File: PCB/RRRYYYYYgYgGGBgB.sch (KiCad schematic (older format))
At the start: 46 parts, among them U1 74HC595, U2 74HC595

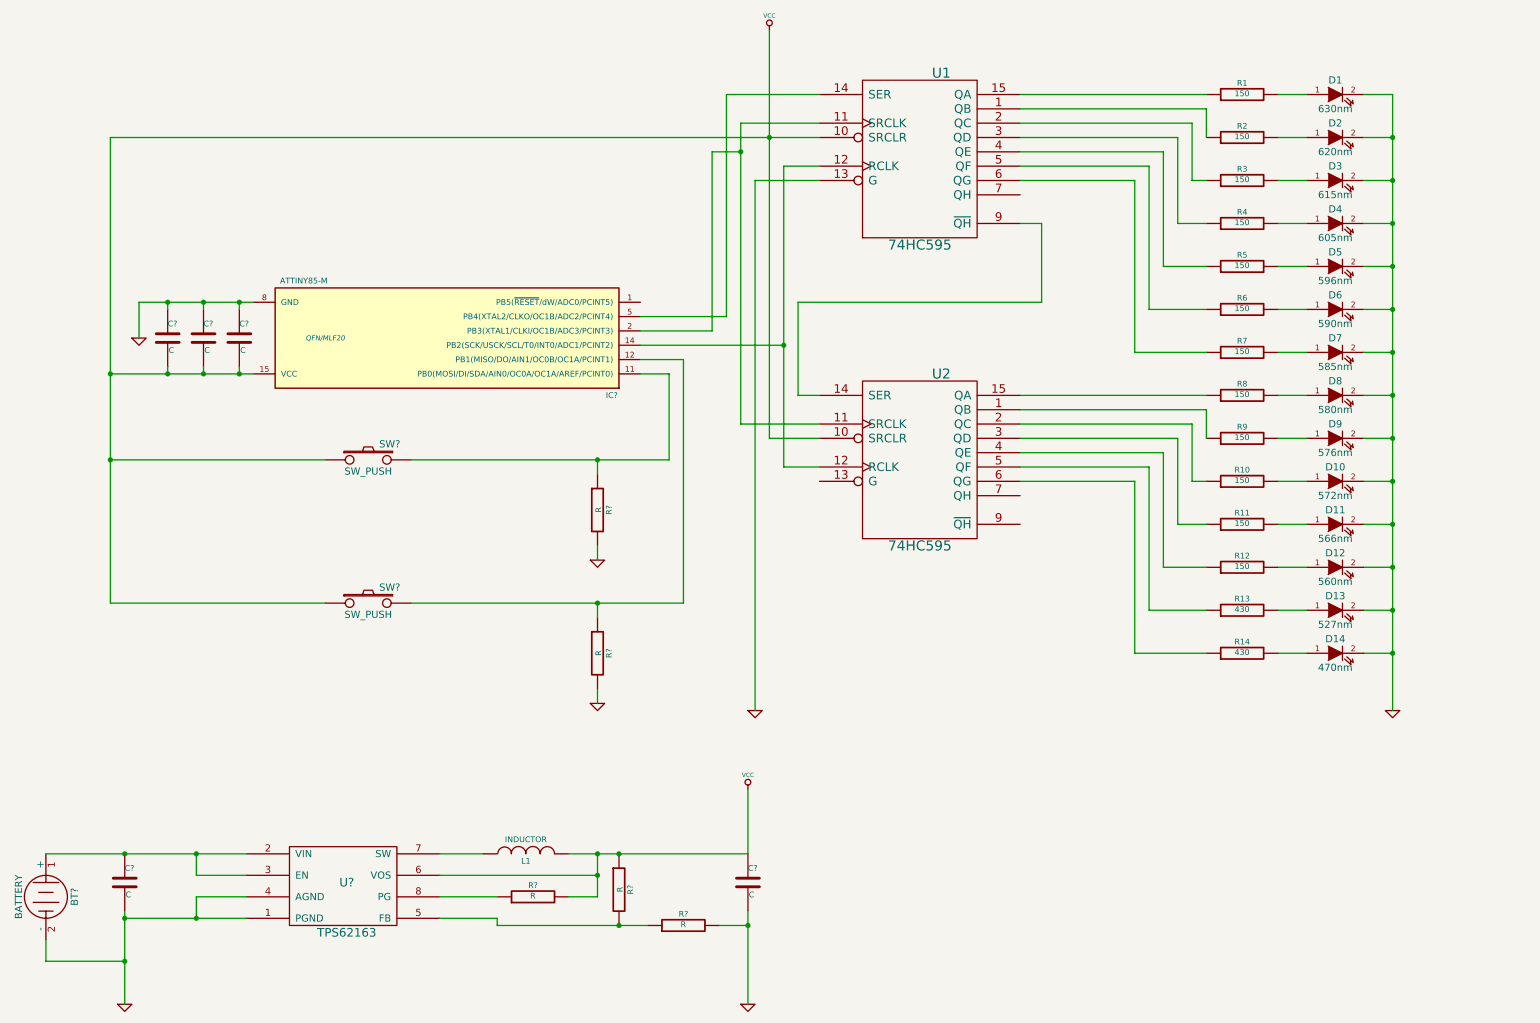
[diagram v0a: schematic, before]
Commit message: Changed from buck to boost converter for 3vdc power. Added values and designators for various components. Generated a netlist. More changes (likely) to come.
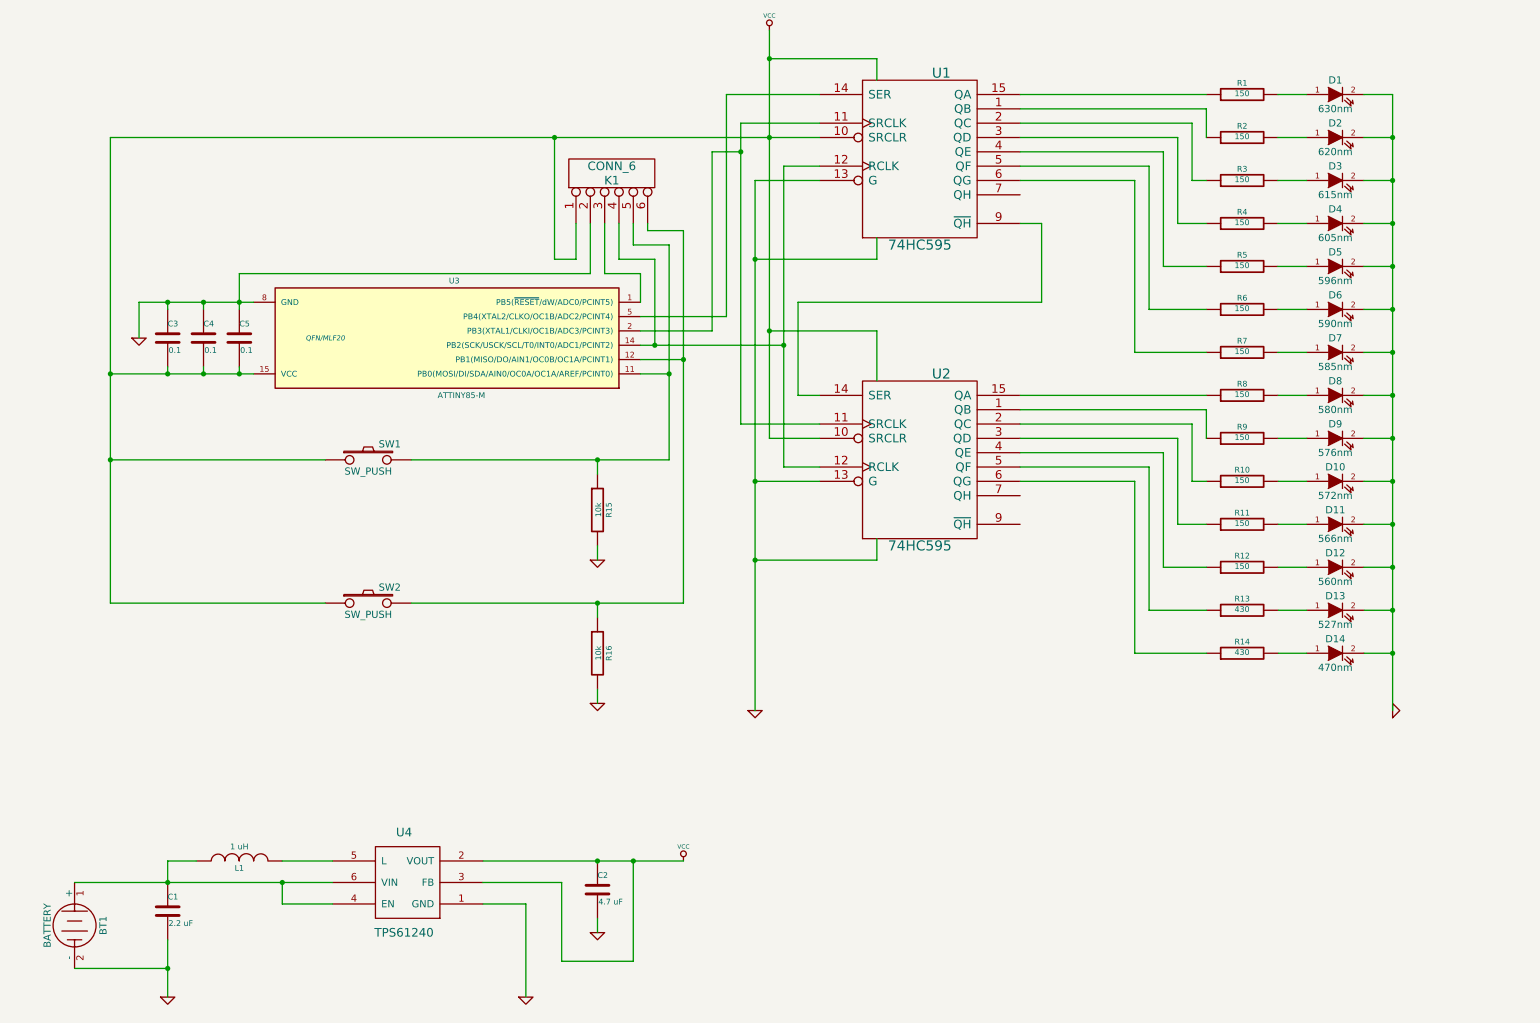
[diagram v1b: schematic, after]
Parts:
- removed BT?: BATTERY, ~, symbol BATTERY
- removed C? (x2): C, ~, symbol C
- removed R? (x3): R, ~, symbol R
- removed U?: TPS62163, symbol TPS62163
- added BT1: BATTERY, ~, symbol BATTERY
- added C1: 2.2 uF, ~, symbol C
- added C2: 4.7 uF, ~, symbol C
- added K1: CONN_6, symbol CONN_6
- added U4: TPS61240, symbol TPS61240
- C3, C4, C5: renamed from C?; value C -> 0.1
- L1: value INDUCTOR -> 1 uH
- R15, R16: renamed from R?; value R -> 10k
- gave numbers to parts that had none: 3
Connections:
- net GND: now also U2.13 (G), BT1.2 (-), C1.2, C2.2, K1.2, U4.1 (GND)
- net VCC: now also C2.1, K1.1, U4.2 (VOUT), U4.3 (FB); no longer L1.2
- net at U1.12 (RCLK), U2.12 (RCLK), U3.14 (PB2(SCK/USCK/SCL/T0/INT0/ADC1/PCINT2)): now also K1.4
- net at U3.1 (PB5(~RESET~/dW/ADC0/PCINT5)): now also K1.3
- net at R15.1, SW1.2, U3.11 (PB0(MOSI/DI/SDA/AIN0/OC0A/OC1A/AREF/PCINT0)): now also K1.5
- net at R16.1, SW2.2, U3.12 (PB1(MISO/DO/AIN1/OC0B/OC1A/PCINT1)): now also K1.6
- net at L1.1: now also BT1.1 (+), C1.1, U4.4 (EN), U4.6 (VIN)
- new net: L1.2, U4.5 (L)

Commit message: added pink and white LEDs. started pcb layout. LEDs arranged in an ~80 degree arc. schematic changed around a bit to make routing a tiny bit easier. note: schematic (specifically around shift registers and LEDs) is now quite difficult to read.
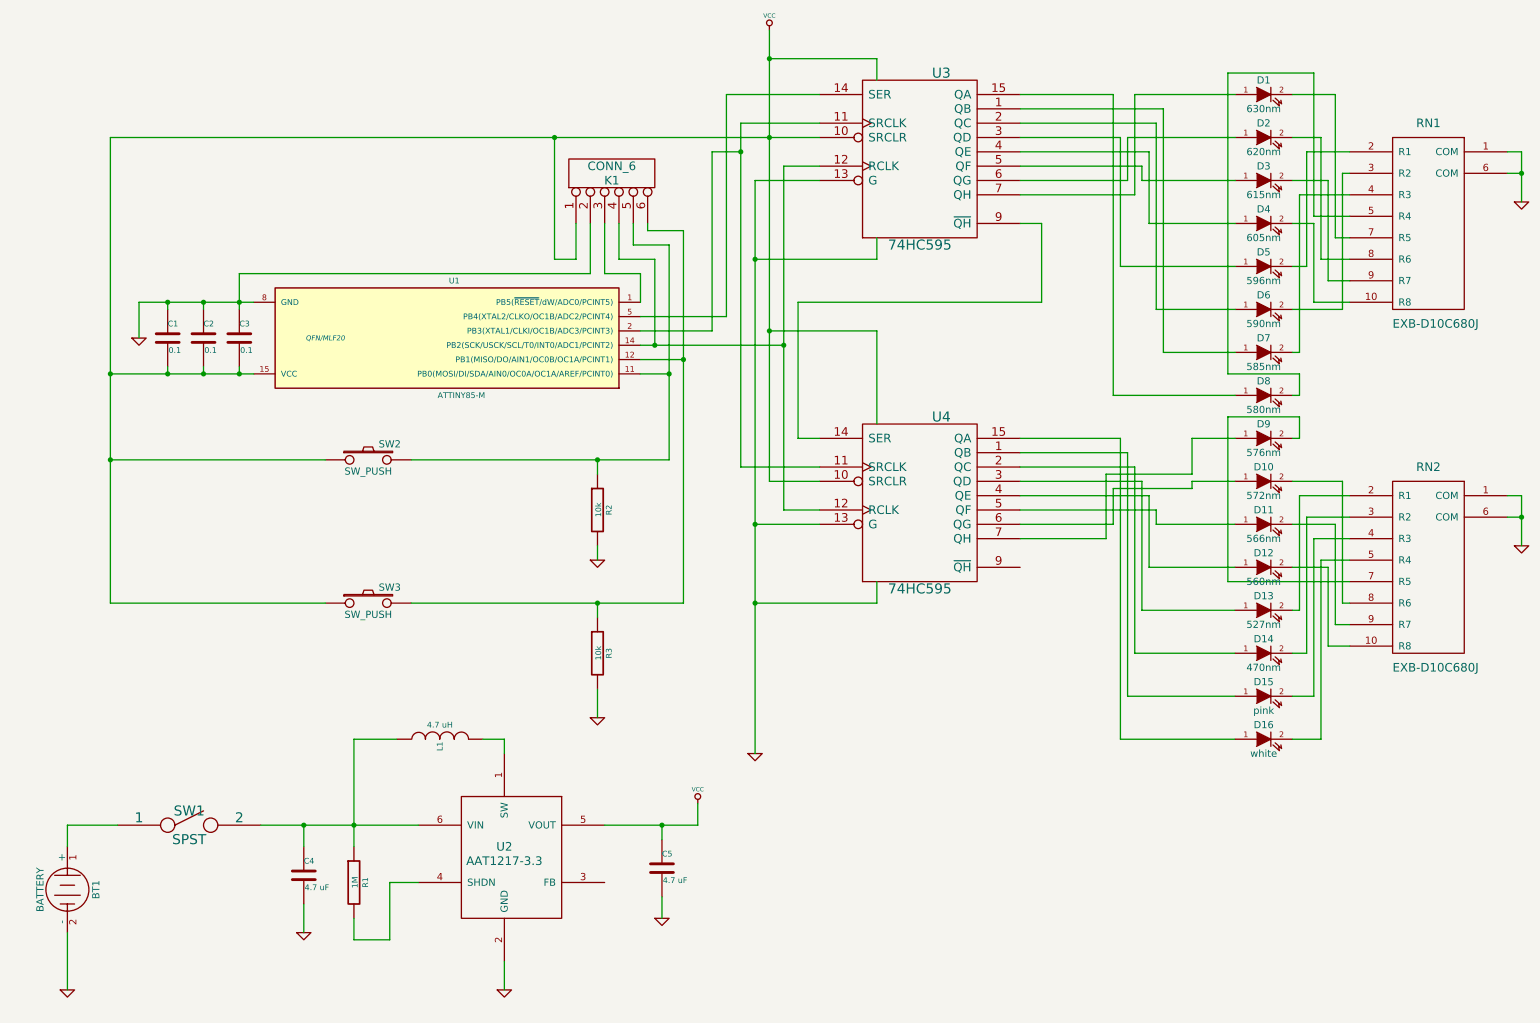
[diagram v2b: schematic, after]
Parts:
- removed C1: 2.2 uF, ~, symbol C
- removed C2: 4.7 uF, ~, symbol C
- removed R10, R11, R12, R2, R3, R4, R5, R6, R7, R8, R9: 150, ~, symbol R
- removed R13, R14: 430, ~, symbol R
- removed U4: TPS61240, symbol TPS61240
- added C4, C5: 4.7 uF, ~, symbol C
- added D15: pink, ~, symbol LED
- added D16: white, ~, symbol LED
- added RN1, RN2: EXB-D10C680J, symbol EXB-D10C680J
- added SW1: SPST, ~, symbol SPST
- added U2: AAT1217-3.3, symbol AAT1217-3.3
- L1: value 1 uH -> 4.7 uH
- R1: value 150 -> 1M
- renumbered C3 to C1, C4 to C2, C5 to C3, R15 to R2, R16 to R3, SW1 to SW2, SW2 to SW3, U3 to U1, U1 to U3, U2 to U4
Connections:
- net GND: now also C4.2, C5.2, RN1.1 (COM), RN1.6 (COM), RN2.1 (COM), RN2.6 (COM), U2.2 (GND); no longer D1.2 (K), D10.2 (K), D11.2 (K), D12.2 (K), D13.2 (K), D14.2 (K), D2.2 (K), D3.2 (K), D4.2 (K), D5.2 (K), D6.2 (K), D7.2 (K), D8.2 (K), D9.2 (K)
- net VCC: now also C5.1, U2.5 (VOUT)
- net at D7.1 (A): now also U3.1 (QB)
- net at D1.1 (A): now also U3.7 (QH); no longer R1.2
- net at D2.1 (A): now also U3.6 (QG)
- net at D3.1 (A): now also U3.5 (QF)
- net at D4.1 (A): now also U3.4 (QE)
- net at D5.1 (A): now also U3.3 (QD)
- net at U3.15 (QA): now also D8.1 (A); no longer R1.1
- net at U3.2 (QC): now also D6.1 (A)
- net at D9.1 (A): now also U4.7 (QH)
- net at D10.1 (A): now also U4.6 (QG)
- net at D11.1 (A): now also U4.5 (QF)
- net at D12.1 (A): now also U4.4 (QE)
- net at D13.1 (A): now also U4.3 (QD)
- net at U4.1 (QB): now also D15.1 (A)
- net at U4.15 (QA): now also D16.1 (A)
- net at U4.2 (QC): now also D14.1 (A)
- net at L1.1: now also R1.1, C4.1, SW1.2, U2.6 (VIN); no longer BT1.1 (+)
- net at L1.2: now also U2.1 (SW)
- new net: D7.2 (K), RN1.4 (R3)
- new net: D1.2 (K), RN1.7 (R5)
- new net: D2.2 (K), RN1.8 (R6)
- new net: D3.2 (K), RN1.9 (R7)
- new net: D4.2 (K), RN1.10 (R8)
- new net: D5.2 (K), RN1.2 (R1)
- new net: D8.2 (K), RN1.5 (R4)
- new net: D9.2 (K), RN2.7 (R5)
- new net: D10.2 (K), RN2.8 (R6)
- new net: D11.2 (K), RN2.9 (R7)
- new net: D12.2 (K), RN2.10 (R8)
- new net: D13.2 (K), RN2.2 (R1)
- new net: D6.2 (K), RN1.3 (R2)
- new net: D14.2 (K), RN2.3 (R2)
- new net: R1.2, U2.4 (SHDN)
- new net: BT1.1 (+), SW1.1
- new net: D15.2 (K), RN2.4 (R3)
- new net: D16.2 (K), RN2.5 (R4)
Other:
- moved on the sheet: D1, D10, D11, D12, D13, D14, D2, D3, D4, D5, D6, D7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
